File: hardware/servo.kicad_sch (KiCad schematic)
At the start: 39 parts, among them J1 Jack-DC, J2 servo, J3 swd, Q1 DMT64M8LSS, SW1 restart, SW2 buzzer, U1 AOZ1284PI, U2 LDI1117-3.3U-DIO, U3 STM32G030F6Px

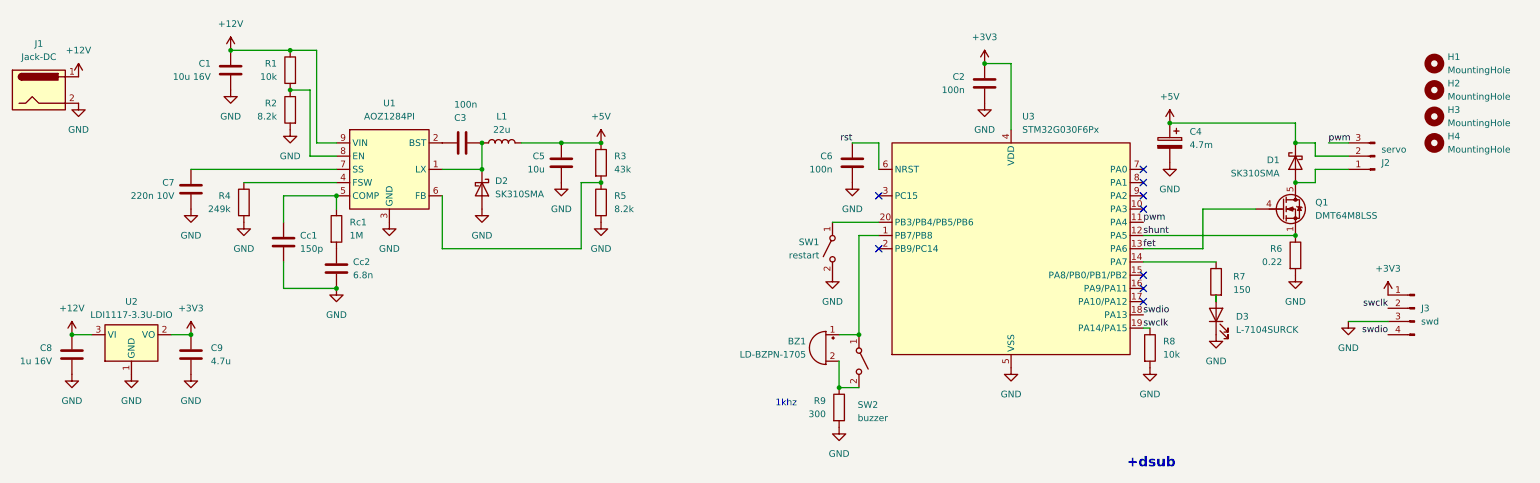
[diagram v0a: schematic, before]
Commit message: Add connector for LEDs, finished PCB picture
Add connector for LED module, finished PCB picture, edit schematic for readability
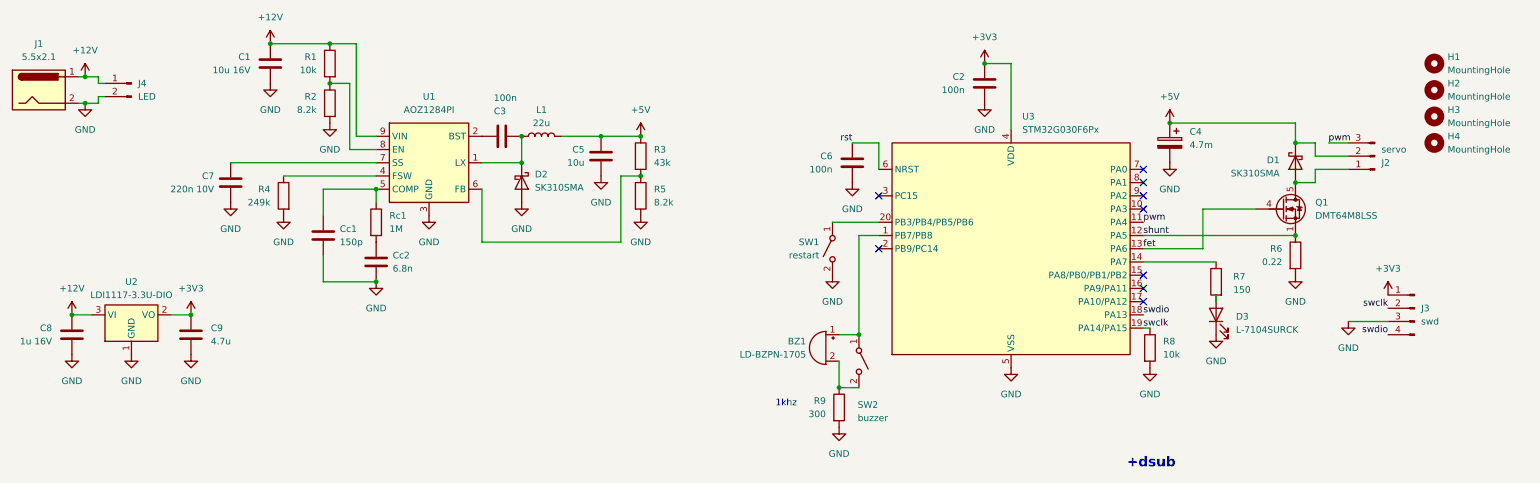
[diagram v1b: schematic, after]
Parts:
- added J4: LED, Connector_Phoenix_MSTB:PhoenixContact_MSTBA_2,5_2-G-5,08_1x02_P5.08mm_Horizontal, symbol Connector:Conn_01x02_Pin
- J1: value Jack-DC -> 5.5x2.1
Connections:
- net +12V: now also J4.1 (Pin_1)
- net GND: now also J4.2 (Pin_2)
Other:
- moved on the sheet: C1, C3, C5, C7, C8, C9, Cc1, Cc2, D2, L1, R1, R2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
